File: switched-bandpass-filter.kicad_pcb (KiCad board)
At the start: 2 copper layers, 114 x 75 mm, 0 parts

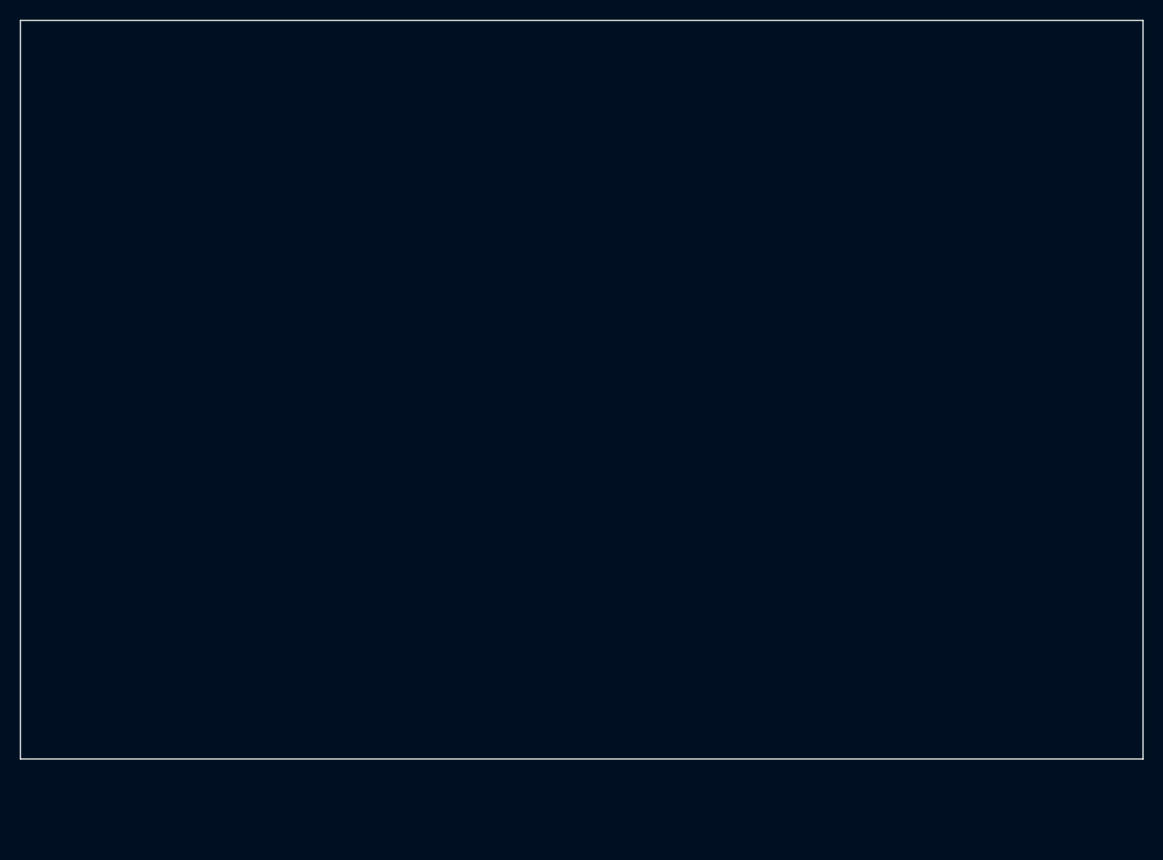
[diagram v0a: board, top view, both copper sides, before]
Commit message: v0.2 passes ERC & DRC except for no solder mask between pads on SOT89
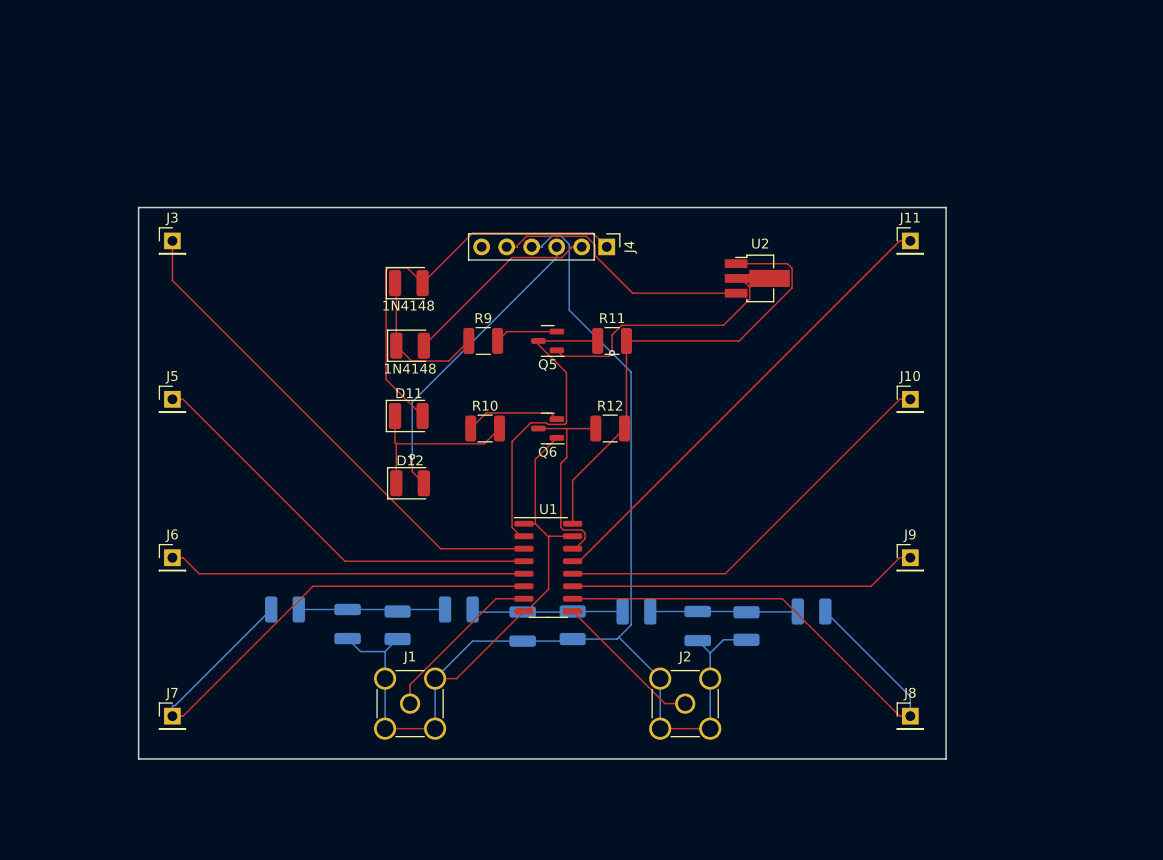
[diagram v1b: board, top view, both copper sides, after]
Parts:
- added C1: C_Polarized_Small_US, Capacitor_SMD:C_1210_3225Metric, B.Cu at (144.8, 111.5)
- added C2: C_Polarized_Small_US, Capacitor_SMD:C_1210_3225Metric, B.Cu at (127.0, 111.6)
- added C3: C_Polarized_Small_US, Capacitor_SMD:C_1210_3225Metric, B.Cu at (109.2, 111.3)
- added D10: 1N4148, Diode_SMD:D_1210_3225Metric, F.Cu at (115.6, 83.0)
- added D11: 1N4148, Diode_SMD:D_1210_3225Metric, F.Cu at (115.4, 90.2)
- added D12: 1N4148, Diode_SMD:D_1210_3225Metric, F.Cu at (115.6, 97.0)
- added D9: 1N4148, Diode_SMD:D_1210_3225Metric, F.Cu at (115.4, 76.7)
- added J1: SMA, Connector_Coaxial:SMA_Amphenol_901-144_Vertical, F.Cu at (115.6, 119.4)
- added J10: F3 out, Connector_PinHeader_2.54mm:PinHeader_1x01_P2.54mm_Vertical, F.Cu at (166.4, 88.5)
- added J11: F4 out, Connector_PinHeader_2.54mm:PinHeader_1x01_P2.54mm_Vertical, F.Cu at (166.4, 72.4)
- added J2: SMA, Connector_Coaxial:SMA_Amphenol_901-144_Vertical, F.Cu at (143.5, 119.4)
- added J3: F4 in, Connector_PinHeader_2.54mm:PinHeader_1x01_P2.54mm_Vertical, F.Cu at (91.4, 72.4)
- added J4: Conn_01x06_Pin, Connector_PinHeader_2.54mm:PinHeader_1x06_P2.54mm_Vertical, F.Cu at (135.5, 73.0)
- added J5: F3 in, Connector_PinHeader_2.54mm:PinHeader_1x01_P2.54mm_Vertical, F.Cu at (91.4, 88.5)
- added J6: F2 in, Connector_PinHeader_2.54mm:PinHeader_1x01_P2.54mm_Vertical, F.Cu at (91.4, 104.6)
- added J7: F1 in, Connector_PinHeader_2.54mm:PinHeader_1x01_P2.54mm_Vertical, F.Cu at (91.4, 120.7)
- added J8: F1 out, Connector_PinHeader_2.54mm:PinHeader_1x01_P2.54mm_Vertical, F.Cu at (166.4, 120.7)
- added J9: F2 out, Connector_PinHeader_2.54mm:PinHeader_1x01_P2.54mm_Vertical, F.Cu at (166.4, 104.6)
- added L1: L, Inductor_SMD:L_1210_3225Metric, B.Cu at (156.3, 110.0)
- added L2: L, Inductor_SMD:L_1210_3225Metric, B.Cu at (138.6, 110.0)
- added L3: L, Inductor_SMD:L_1210_3225Metric, B.Cu at (120.5, 109.8)
- added L4: L, Inductor_SMD:L_1210_3225Metric, B.Cu at (102.9, 109.8)
- added L5: L, Inductor_SMD:L_1210_3225Metric, B.Cu at (149.7, 111.5)
- added L6: L, Inductor_SMD:L_1210_3225Metric, B.Cu at (132.1, 111.4)
- added L7: L, Inductor_SMD:L_1210_3225Metric, B.Cu at (114.3, 111.4)
- added Q5: 2N3904, Package_TO_SOT_SMD:SOT-23, F.Cu at (129.5, 82.5)
- added Q6: 2N3904, Package_TO_SOT_SMD:SOT-23, F.Cu at (129.5, 91.4)
- added R10: 4.7K, Resistor_SMD:R_1210_3225Metric, F.Cu at (123.2, 91.4)
- added R11: 10K, Resistor_SMD:R_1210_3225Metric, F.Cu at (136.1, 82.5)
- added R12: 10K, Resistor_SMD:R_1210_3225Metric, F.Cu at (135.9, 91.4)
- added R9: 4.7K, Resistor_SMD:R_1210_3225Metric, F.Cu at (123.0, 82.5)
- added U1: FST3253MX, Package_SO:SOIC-16_3.9x9.9mm_P1.27mm, F.Cu at (129.6, 105.6)
- added U2: L78L05_SOT89, Package_TO_SOT_SMD:SOT-89-3_Handsoldering, F.Cu at (151.1, 76.2)
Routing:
- net GND: track 0.00 -> 184.0 mm, vias 0 -> 1
- net F1 in: track 0.00 -> 56.3 mm
- net F1 out: track 0.00 -> 53.4 mm
- net F4 in: track 0.00 -> 51.0 mm
- net F4 out: track 0.00 -> 47.8 mm
- net +5V: track 0.00 -> 47.7 mm
- net F3 in: track 0.00 -> 42.5 mm
- net P1: track 0.00 -> 42.1 mm
- net F3 out: track 0.00 -> 41.6 mm
- net F2 in: track 0.00 -> 36.4 mm
- net F2 out: track 0.00 -> 35.5 mm
- net S1: track 0.00 -> 32.3 mm
- net P3: track 0.00 -> 30.6 mm, vias 0 -> 1
- net +12V: track 0.00 -> 26.8 mm
- net S0: track 0.00 -> 21.1 mm
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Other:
- board size 114 x 75 mm -> 82 x 56 mm

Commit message: v0.3 added all four filters.  ERC pass, DRC struggling.  Need a ground plane
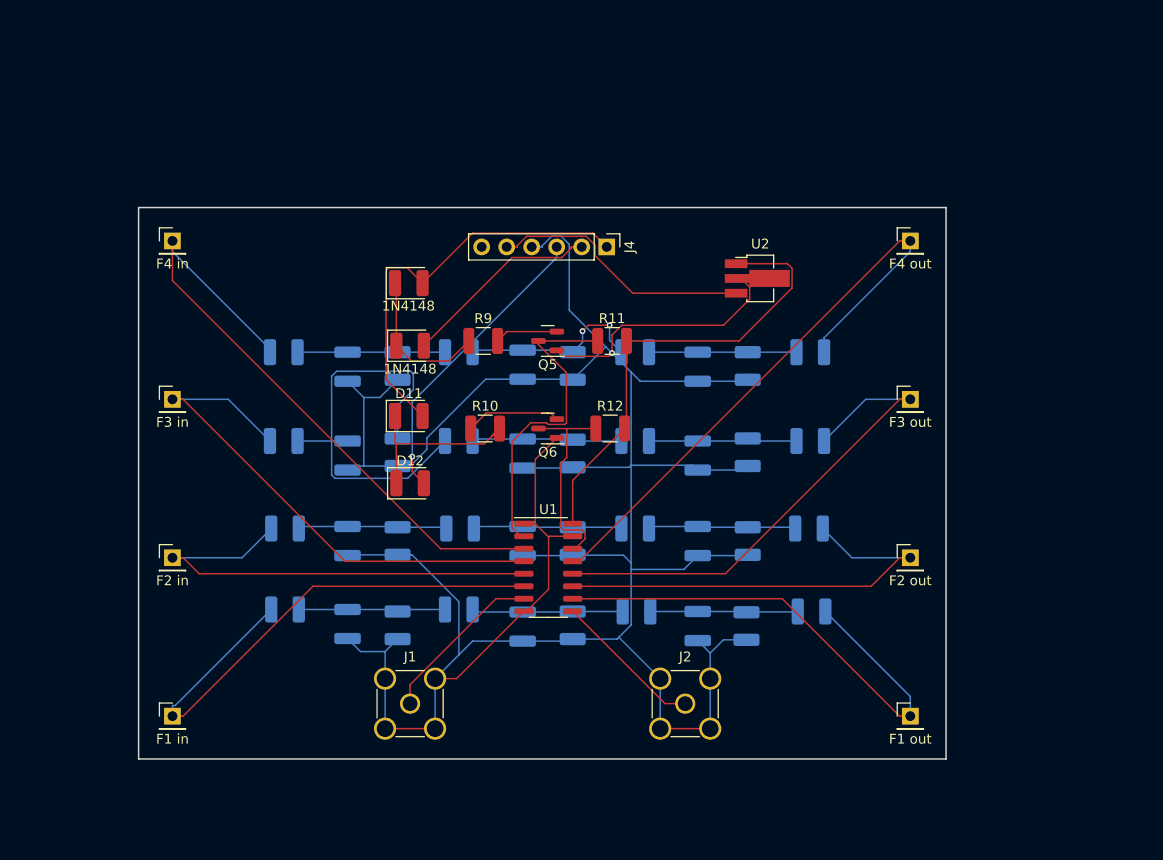
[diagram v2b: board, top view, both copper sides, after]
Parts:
- added C10: , Capacitor_SMD:C_1210_3225Metric, B.Cu at (127.0, 85.0)
- added C11: , Capacitor_SMD:C_1210_3225Metric, B.Cu at (109.2, 94.2)
- added C12: , Capacitor_SMD:C_1210_3225Metric, B.Cu at (109.2, 85.2)
- added C4: , Capacitor_SMD:C_1210_3225Metric, B.Cu at (144.8, 102.9)
- added C5: , Capacitor_SMD:C_1210_3225Metric, B.Cu at (127.0, 102.9)
- added C6: , Capacitor_SMD:C_1210_3225Metric, B.Cu at (109.2, 102.9)
- added C7: , Capacitor_SMD:C_1210_3225Metric, B.Cu at (144.8, 94.2)
- added C8: , Capacitor_SMD:C_1210_3225Metric, B.Cu at (144.8, 85.2)
- added C9: , Capacitor_SMD:C_1210_3225Metric, B.Cu at (127.0, 94.0)
- added L10: L, Inductor_SMD:L_1210_3225Metric, B.Cu at (138.4, 101.6)
- added L11: L, Inductor_SMD:L_1210_3225Metric, B.Cu at (132.1, 102.9)
- added L12: L, Inductor_SMD:L_1210_3225Metric, B.Cu at (120.7, 101.6)
- added L13: L, Inductor_SMD:L_1210_3225Metric, B.Cu at (114.3, 102.9)
- added L14: L, Inductor_SMD:L_1210_3225Metric, B.Cu at (102.9, 101.6)
- added L15: L, Inductor_SMD:L_1210_3225Metric, B.Cu at (156.2, 92.7)
- added L16: L, Inductor_SMD:L_1210_3225Metric, B.Cu at (156.2, 83.7)
- added L17: L, Inductor_SMD:L_1210_3225Metric, B.Cu at (149.9, 93.8)
- added L18: L, Inductor_SMD:L_1210_3225Metric, B.Cu at (149.9, 85.1)
- added L19: L, Inductor_SMD:L_1210_3225Metric, B.Cu at (138.4, 92.7)
- added L20: L, Inductor_SMD:L_1210_3225Metric, B.Cu at (138.4, 83.7)
- added L21: L, Inductor_SMD:L_1210_3225Metric, B.Cu at (132.1, 94.0)
- added L22: L, Inductor_SMD:L_1210_3225Metric, B.Cu at (132.1, 85.1)
- added L23: L, Inductor_SMD:L_1210_3225Metric, B.Cu at (120.5, 92.7)
- added L24: L, Inductor_SMD:L_1210_3225Metric, B.Cu at (120.5, 83.7)
- added L25: L, Inductor_SMD:L_1210_3225Metric, B.Cu at (114.3, 93.8)
- added L26: L, Inductor_SMD:L_1210_3225Metric, B.Cu at (114.3, 85.1)
- added L27: L, Inductor_SMD:L_1210_3225Metric, B.Cu at (102.7, 92.7)
- added L28: L, Inductor_SMD:L_1210_3225Metric, B.Cu at (102.7, 83.7)
- added L8: L, Inductor_SMD:L_1210_3225Metric, B.Cu at (156.1, 101.6)
- added L9: L, Inductor_SMD:L_1210_3225Metric, B.Cu at (149.9, 102.9)
- C1, C2, C3: value C_Polarized_Small_US -> (none)
- J4: value Conn_01x06_Pin -> (none)
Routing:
- net GND: track 184.0 -> 308.2 mm
- net Net-(C11-Pad1): track 0.00 -> 44.2 mm
- net Net-(C10-Pad1): track 0.00 -> 19.1 mm, vias 0 -> 2
- net F4 in: track 51.0 -> 66.4 mm
- net Net-(C9-Pad1): track 0.00 -> 15.3 mm
- net Net-(C7-Pad1): track 0.00 -> 15.2 mm
- net Net-(C5-Pad1): track 0.00 -> 15.1 mm
- net Net-(C6-Pad1): track 0.00 -> 15.1 mm
- net Net-(C4-Pad1): track 0.00 -> 15.0 mm
- net Net-(C12-Pad1): track 0.00 -> 15.0 mm
- net Net-(C8-Pad1): track 0.00 -> 15.0 mm
- net F4 out: track 47.8 -> 62.7 mm
- net F3 in: track 42.5 -> 54.2 mm
- net F2 in: track 36.4 -> 47.6 mm
- net F3 out: track 41.6 -> 52.1 mm
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
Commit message: v0.3 ERC pass, DRC two unconnected.  Stitching ground planes may solve this.
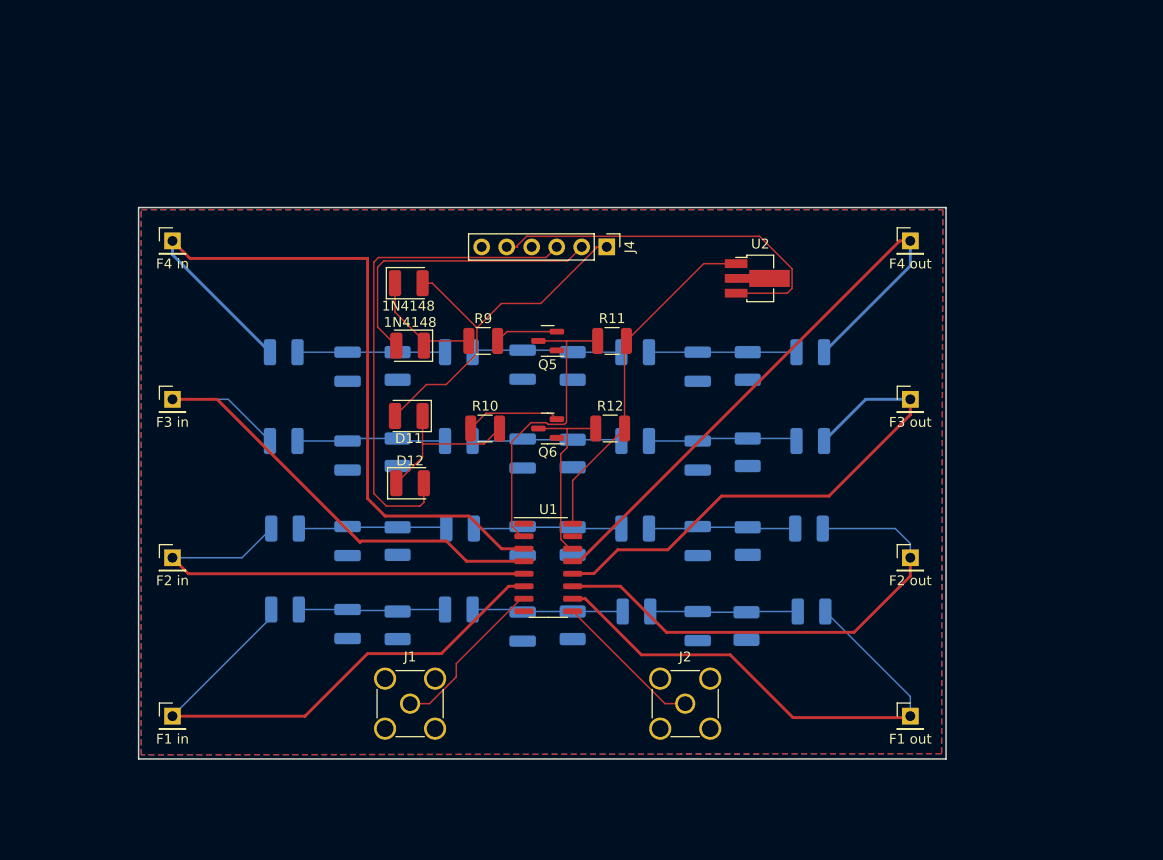
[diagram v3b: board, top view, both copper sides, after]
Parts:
- turned D10 to 180 degrees
- turned D11 to 180 degrees
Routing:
- net GND: track 308.2 -> 0.00 mm, vias 1 -> 0
- net Net-(C11-Pad1): track 44.2 -> 15.2 mm
- net P3: track 30.6 -> 50.4 mm, vias 1 -> 0
- net +5V: track 47.7 -> 35.2 mm
- net F4 in: track 66.4 -> 78.3 mm
- net +12V: track 26.8 -> 38.8 mm
- net P2: track 20.3 -> 30.3 mm
- net F2 out: track 45.6 -> 51.4 mm
- net P1: track 42.1 -> 37.6 mm
- net Net-(C10-Pad1): track 19.1 -> 15.3 mm, vias 2 -> 0
- net Net-(D10-K): track 15.3 -> 12.1 mm
- net Net-(D11-K): track 19.1 -> 16.4 mm
- net S0: track 21.1 -> 18.9 mm
- net S1: track 32.3 -> 31.0 mm
- net Net-(Q6-B): track 10.8 -> 9.64 mm
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- added copper zone on B.Cu, net GND
- added copper zone on F.Cu, net GND

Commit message: v0.3 ERC/DRC pass; via stitch in place.  Time for a squint
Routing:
- net GND: track 0.00 -> 5.27 mm, vias 0 -> 282
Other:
- board text added: "N7TDB"
- board text added: "switched bandpass filter v0.3 Copyright © 2023 WA7GIL"

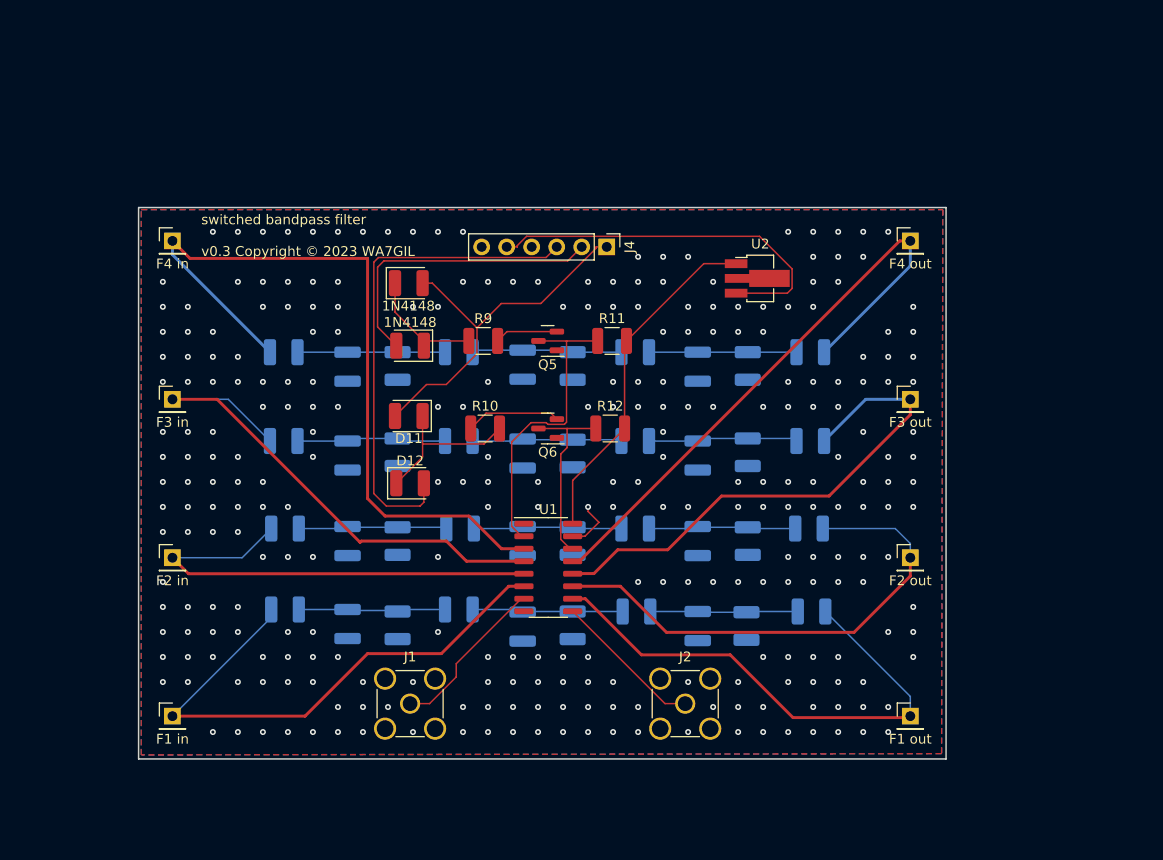
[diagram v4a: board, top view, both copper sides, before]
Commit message: v0.4 ERC/DRC pass; added missing caps; mounting holes; moved SMA & headers out and re-spaced filter chains
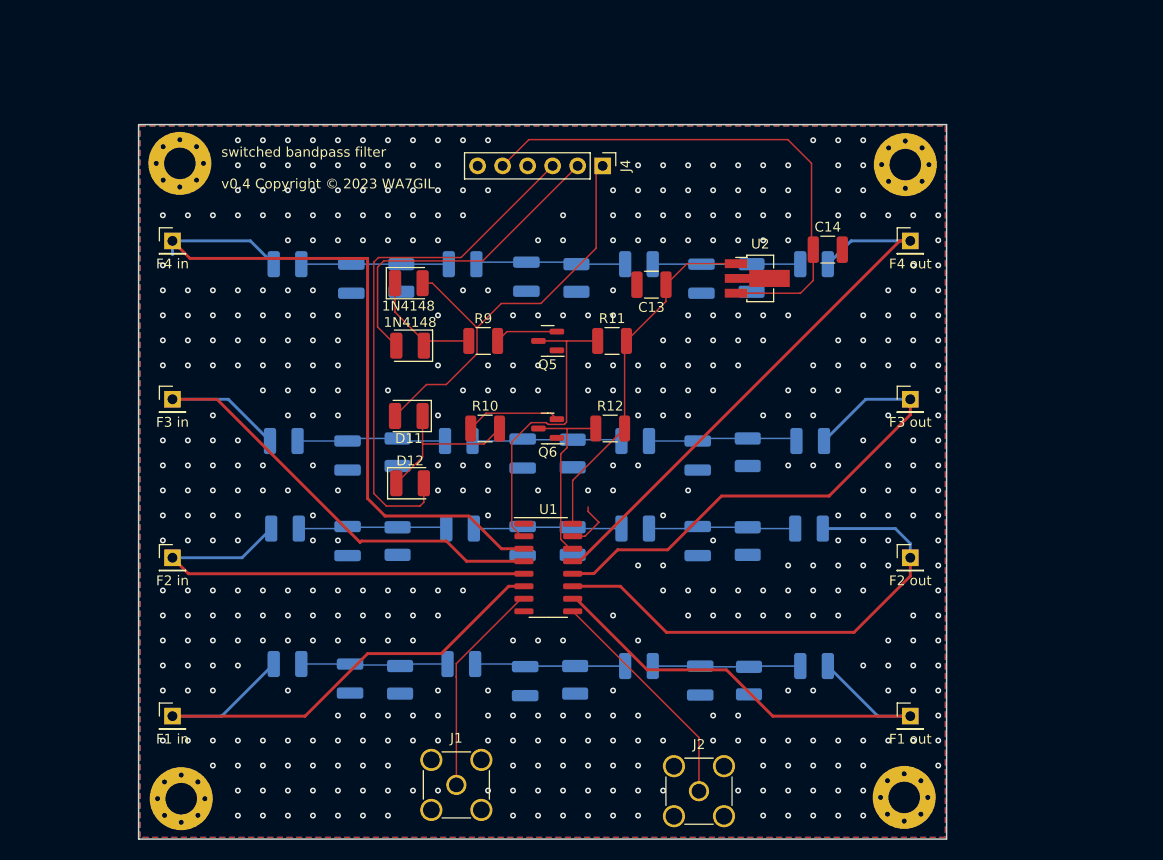
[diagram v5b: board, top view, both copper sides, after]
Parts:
- added C13: 0.1 uF, Capacitor_SMD:C_1210_3225Metric, F.Cu at (140.1, 76.8)
- added C14: 10 uF, Capacitor_SMD:C_1210_3225Metric, F.Cu at (158.0, 73.3)
- added H1: , MountingHole:MountingHole_3.2mm_M3_Pad_Via, F.Cu at (92.2, 64.5)
- added H2: , MountingHole:MountingHole_3.2mm_M3_Pad_Via, F.Cu at (165.9, 64.6)
- added H3: , MountingHole:MountingHole_3.2mm_M3_Pad_Via, F.Cu at (165.7, 128.9)
- added H4: , MountingHole:MountingHole_3.2mm_M3_Pad_Via, F.Cu at (92.3, 129.0)
- moved J1 9.50 mm to (120.3, 127.6)
- moved J2 9.00 mm to (144.9, 128.3)
- moved C12 8.94 mm to (109.6, 76.2)
- moved C8 8.94 mm to (145.2, 76.2)
- moved L26 8.94 mm to (114.7, 76.2)
- moved L18 8.94 mm to (150.2, 76.2)
- moved L22 8.94 mm to (132.5, 76.2)
- moved C10 8.94 mm to (127.4, 76.0)
- moved L16 8.94 mm to (156.6, 74.8)
- moved L20 8.94 mm to (138.8, 74.8)
- moved L24 8.94 mm to (120.9, 74.8)
- moved L28 8.94 mm to (103.1, 74.8)
- moved J4 8.24 mm to (135.1, 64.8)
- moved L5 5.54 mm to (150.0, 117.0)
- moved C1 5.54 mm to (145.0, 117.0)
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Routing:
- net +12V: track 38.8 -> 53.8 mm
- net F2 common: track 15.3 -> 23.6 mm
- net P1: track 37.6 -> 45.1 mm
- net F4 out: track 62.7 -> 57.1 mm
- net F1 common: track 16.8 -> 21.9 mm
- net F1 out: track 53.5 -> 49.7 mm
- net P3: track 50.4 -> 53.4 mm
- net P2: track 30.3 -> 33.3 mm
- net F4 in: track 78.3 -> 75.6 mm
- net F1 in: track 56.1 -> 53.6 mm
- net +5V: track 35.2 -> 36.2 mm
- net GND: vias 282 -> 474
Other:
- board size 82 x 56 mm -> 82.1 x 72.6 mm
- board text added: "F1 in"
- board text added: "F1 out"
- board text added: "F2 in"
- board text added: "F2 out"
- board text added: "F3 in"
- board text added: "F3 out"
- board text added: "F4 in"
- board text added: "F4 out"
- board text added: "switched bandpass filter v0.4 Copyright © 2023 WA7GIL"
- board text removed: "switched bandpass filter v0.3 Copyright © 2023 WA7GIL"
